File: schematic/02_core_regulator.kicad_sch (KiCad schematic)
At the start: 24 parts, among them U201 TPS546B24ARVFR

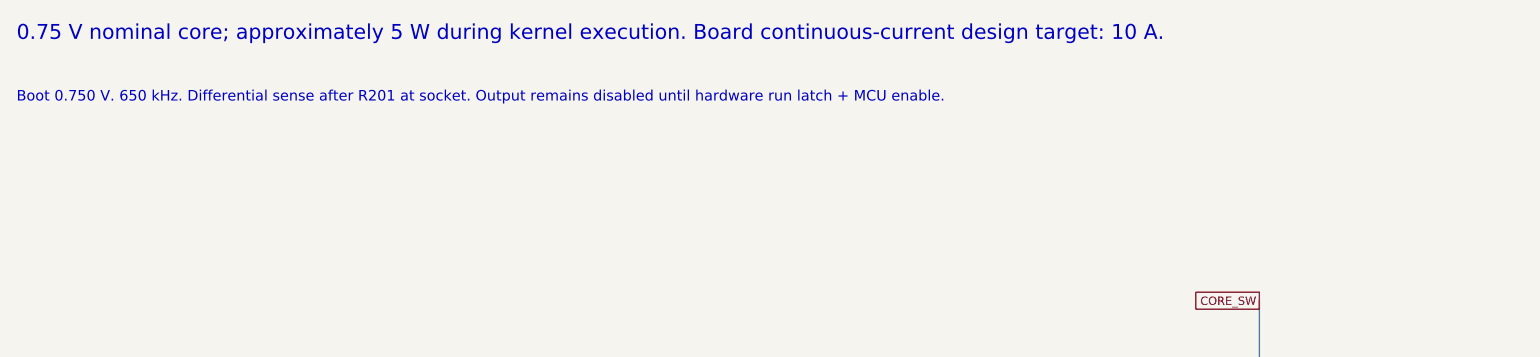
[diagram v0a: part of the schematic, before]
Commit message: Make V2 power state independent of Pico
Add an independently powered retained control domain, isolated I2C, hardware temperature and I/O overvoltage protection, and correct the socket keepout. Align operating requirements, BOM, schematic exports, and validation evidence.

Complete the final source review: zero ERC violations, 247 footprint/BOM matches, 80 ASIC pin checks, and 51 companion host tests including 122 interrupted-write cases. Record physical qualification limits and external companion firmware hashes.
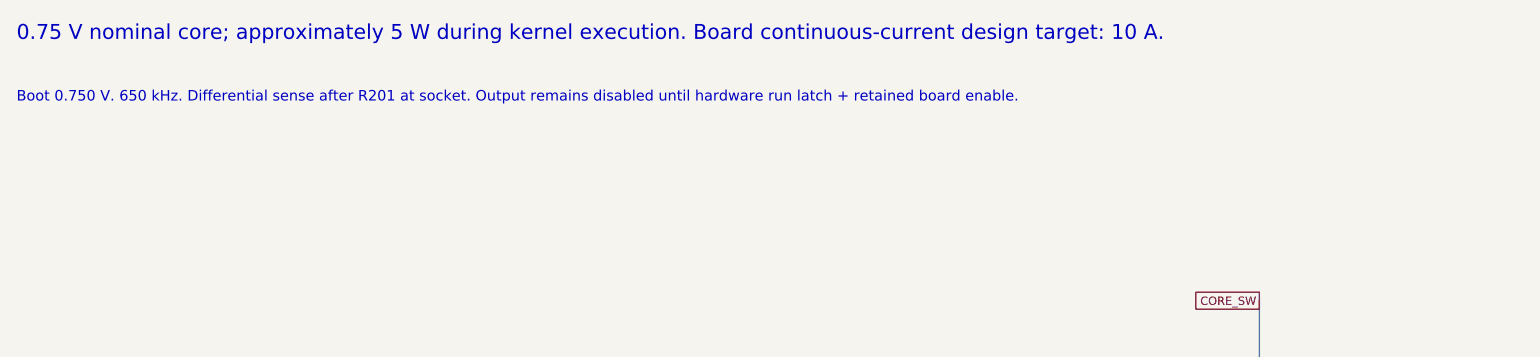
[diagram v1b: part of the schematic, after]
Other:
- note added: "Boot 0.750 V. 650 kHz. Differential sense after R201 at socket. Output remains disabled until hardware run latch + retained board enable."
- note removed: "Boot 0.750 V. 650 kHz. Differential sense after R201 at socket. Output remains disabled until hardware run latch + MCU enable."
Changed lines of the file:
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@@
         (comment 3 "Author: Yuchen Mei"))
         (text "0.75 V nominal core; approximately 5 W during kernel execution. Board continuous-current design target: 10 A." (at 15 15 0) (effects (font (size 1.8 1.8)) (justify left top) ))
-(text "Boot 0.750 V. 650 kHz. Differential sense after R201 at socket. Output remains disabled until hardware run latch + MCU enable." (at 15 23 0) (effects (font (size 1.27 1.27)) (justify left top) ))
+(text "Boot 0.750 V. 650 kHz. Differential sense after R201 at socket. Output remains disabled until hardware run latch + retained board enable." (at 15 23 0) (effects (font (size 1.27 1.27)) (justify left top) ))
 (symbol (lib_id "Sphinx_V2:TPS546B24A") (at 100.33 115.57 0) (unit 1) (exclude_from_sim no) (in_bom yes) (on_board yes) (dnp no)
 (property "Reference" "U201" (at 100.33 63.85 0) (effects (font (size 1.0 1.0))  ))
